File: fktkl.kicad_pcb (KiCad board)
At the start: 2 copper layers, 345.7 x 94.2 mm, 158 parts, among them K1 Esc, K10 Super, K11 2, K12 W, K13 S, K14 X, K15 Alt, K16 3, K17 E, K18 D, K19 C, K2 Tab, K20 4, K21 R, K22 F, K23 V, K24 5, K25 T, K26 G, K27 B, K28 6, K29 Y, K3 Caps, K3.1 SCaps, K30 H, K31 N, K32 Space, K33 7, K34 U, K35 J, K36 M, K37 8, K38 I, K39 K, K4 Shift, K40 ,, K41 9, K42 O, K43 L, K44 ., K45 0, K46 P, K47 ;, K48 /, K49 Ctrl, K5 Ctrl, K50 -, K51 [, K52 ', K53 =, K54 ], K55 Shift, K56 Win, K57 Yen, K58 BS1, K59 BS2, K6 1, K60 \, K61 Enter, K62 Fn, K63 AltGr, K64 Ins, K65 Del, K66 C0, K67 C3, K68 Left, K69 Home, K7 Q, K70 End, K71 C1, K72 Up, K73 Down, K74 PgUp, K75 PgDwn, K76 C2, K77 C4, K78 Right, K8 A, K9 Z

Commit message: changed controller to pro micro
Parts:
- removed the K26 at (156.0, 83.4)
- removed K3.1: SCaps, canadian_footprints:Mx_Alps_125
- removed the K49 at (179.8, 121.5)
- removed the K49 at (260.7, 121.5)
- added G***: LOGO, jan_footprints:dachshund_14.1X8.7_COPPER, F.Cu at (240.0, 119.4)
- added G***: LOGO, jan_footprints:dachshund_181.4x111.4, B.Cu at (186.2, 80.0)
- added K26: Space, canadian_footprints:Mx_Alps_150, F.Cu at (173.8, 116.8)
- added K26: AltGr, canadian_footprints:Mx_Alps_150, F.Cu at (254.8, 116.7)
- added K49: L, canadian_footprints:Mx_Alps_100, F.Cu at (226.2, 78.6)
- added REF**: MountingHole_2.5mm, Mounting_Holes:MountingHole_2.5mm, F.Cu at (100.3, 186.4)
- added Reset1: SW_Push, canadian_footprints:SW_TACT_ALPS_SKQGABE010, B.Cu at (356.4, 50.0)
- K1: value Esc -> SCaps; footprint canadian_footprints:Mx_Alps_100 -> canadian_footprints:Mx_Alps_125
- K10: value Super -> Z
- K11: value 2 -> Super
- K12: value W -> 2
- K13: value S -> W
- K14: value X -> S
- K15: value Alt -> X; footprint canadian_footprints:Mx_Alps_150 -> canadian_footprints:Mx_Alps_100
- K16: value 3 -> Alt; footprint canadian_footprints:Mx_Alps_100 -> canadian_footprints:Mx_Alps_150
- K17: value E -> 3
- K18: value D -> E
- K19: value C -> D
- K2: value Tab -> Esc; footprint canadian_footprints:Mx_Alps_150 -> canadian_footprints:Mx_Alps_100
- K20: value 4 -> C
- K21: value R -> Space; footprint canadian_footprints:Mx_Alps_100 -> MX_Alps_Hybrid:MX-7U-ReversedStabilizers-NoLED
- K22: value F -> 4
- K23: value V -> R
- K24: value 5 -> F
- K25: value T -> V
- K27: value B -> 5
- K28: value 6 -> T
- K29: value Y -> G
- K3: value Caps -> Tab; footprint canadian_footprints:Mx_Alps_175 -> canadian_footprints:Mx_Alps_150
- K30: value H -> B
- K31: value N -> Ctrl; footprint canadian_footprints:Mx_Alps_100 -> canadian_footprints:Mx_Alps_150
- K32: value Space -> 6; footprint MX_Alps_Hybrid:MX-7U-ReversedStabilizers-NoLED -> canadian_footprints:Mx_Alps_100
- K33: value 7 -> Y
- K34: value U -> H
- K35: value J -> N
- K36: value M -> Super
- K37: value 8 -> 7
- K38: value I -> U
- K39: value K -> J
- K4: value Shift -> Caps; footprint canadian_footprints:Mx_Alps_225 -> canadian_footprints:Mx_Alps_175
- K40: value , -> M
- K41: value 9 -> Left
- K42: value O -> 8
- K43: value L -> I
- K44: value . -> K
- K45: value 0 -> ,
- K46: value P -> Down
- K47: value ; -> 9
- K48: value / -> O
- K5: value Ctrl -> Shift; footprint canadian_footprints:Mx_Alps_150 -> canadian_footprints:Mx_Alps_225
- K50: value - -> .
- K51: value [ -> Right
- K52: value ' -> 0
- K53: value = -> P
- K54: value ] -> :
- K55: value Shift -> -; footprint canadian_footprints:Mx_Alps_175 -> canadian_footprints:Mx_Alps_100
- K56: value Win -> [
- K57: value Yen -> "
- K58: value BS1 -> =
- K59: value BS2 -> ]; footprint canadian_footprints:Mx_Alps_200 -> canadian_footprints:Mx_Alps_100
- K6: value 1 -> Ctrl; footprint canadian_footprints:Mx_Alps_100 -> canadian_footprints:Mx_Alps_150
- K60: value \ -> /; footprint canadian_footprints:Mx_Alps_150 -> canadian_footprints:Mx_Alps_100
- K61: value Enter -> Yen; footprint canadian_footprints:Mx_Alps_225 -> canadian_footprints:Mx_Alps_100
- K62: value Fn -> |; footprint canadian_footprints:Mx_Alps_100 -> canadian_footprints:Mx_Alps_150
- K63: value AltGr -> Shift; footprint canadian_footprints:Mx_Alps_150 -> canadian_footprints:Mx_Alps_175
- K64: value Ins -> BS
- K66: value C0 -> Fn
- K67: value C3 -> Ins
- K68: value Left -> Enter; footprint canadian_footprints:Mx_Alps_100 -> canadian_footprints:Mx_Alps_225
- K69: value Home -> C3
- K7: value Q -> 1
- K70: value End -> Home
- K71: value C1 -> C0
- K73: value Down -> PgUp
- K74: value PgUp -> C1
- K75: value PgDwn -> C4
- K76: value C2 -> End
- K77: value C4 -> C2
- K78: value Right -> PgDwn
- K8: value A -> Q
- K9: value Z -> A
- U1: value (none) -> ProMicro; footprint jan_footprints:Teensy_20_wo_front_text -> canadian_footprints:Pro_Micro
- moved U1 275.1 mm to (331.0, 44.7), turned to 180 degrees
- moved K41 133.8 mm to (331.0, 116.7)
- moved D45 132.5 mm to (358.1, 116.6)
- moved D30 131.7 mm to (311.9, 116.7)
- moved D50 119.3 mm to (361.2, 116.6)
- moved K31 118.7 mm to (302.4, 116.7)
- moved D25 116.1 mm to (264.3, 116.7)
- moved K46 116.1 mm to (350.0, 116.7)
- moved K51 116.1 mm to (369.1, 116.7)
- moved D40 109.3 mm to (340.5, 116.7)
- moved D35 90.9 mm to (288.1, 116.7)
- moved D20 87.9 mm to (183.4, 116.7)
- moved K32 84.8 mm to (154.8, 40.5)
- moved K73 82.0 mm to (369.1, 40.5)
- moved D72 81.1 mm to (361.2, 40.4)
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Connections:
- D20 pad 1: /row0 -> /row4
- D21 pad 1: /row1 -> /row0
- D22 pad 1: /row2 -> /row1
- D23 pad 1: /row3 -> /row2
- D24 pad 1: /row0 -> /row3
- D25 pad 1: /row1 -> /row4
- D26 pad 1: /row2 -> /row0
- D27 pad 1: /row3 -> /row1
- D28 pad 1: /row0 -> /row2
- D29 pad 1: /row1 -> /row3
- D30 pad 1: /row2 -> /row4
- D31 pad 1: /row3 -> /row0
- D32 pad 1: /row4 -> /row1
- D33 pad 1: /row0 -> /row2
- D34 pad 1: /row1 -> /row3
- D35 pad 1: /row2 -> /row4
- D36 pad 1: /row3 -> /row0
- D37 pad 1: /row0 -> /row1
- D38 pad 1: /row1 -> /row2
- D39 pad 1: /row2 -> /row3
- D40 pad 1: /row3 -> /row4
- D45 pad 1: /row0 -> /row4
- D46 pad 1: /row1 -> /row0
- D47 pad 1: /row2 -> /row1
- D48 pad 1: /row3 -> /row2
- D49 pad 1: /row4 -> /row3
- D50 pad 1: /row0 -> /row4
- D51 pad 1: /row1 -> /row5
- D52 pad 1: /row2 -> /row6
- D53 pad 1: /row0 -> /row7
- D54 pad 1: /row1 -> /row5
- D55 pad 1: /row3 -> /row6
- D56 pad 1: /row4 -> /row7
- D57 pad 1: /row2 -> /row5
- D58 pad 1: /row0 -> /row6
- D59 pad 1: /row1 -> /row7
- D60 pad 1: /row2 -> /row5
- D61 pad 1: /row3 -> /row6
- D62 pad 1: /row4 -> /row7
- D63 pad 1: /row0 -> /row5
- D64 pad 1: /row1 -> /row6
- D65 pad 1: /row2 -> /row7
- D66 pad 1: /row3 -> /row5
- D67 pad 1: /row4 -> /row6
- D68 pad 1: /row0 -> /row7
- D69 pad 1: /row1 -> /row5
- D70 pad 1: /row2 -> /row6
- D71 pad 1: /row3 -> /row7
- D72 pad 1: /row4 -> /row5
- D73 pad 1: /row0 -> /row6
- D74 pad 1: /row1 -> /row7
- D75 pad 1: /row2 -> /row5
- D76 pad 1: /row3 -> /row6
- D77 pad 1: /row4 -> /row5
- K1 pad 2: Net-(D1-Pad2) -> Net-(D3-Pad2)
- K10 pad 2: Net-(D10-Pad2) -> Net-(D9-Pad2)
- K11 pad 1: /col2 -> /col1
- K11 pad 2: Net-(D11-Pad2) -> Net-(D10-Pad2)
- K12 pad 2: Net-(D12-Pad2) -> Net-(D11-Pad2)
- K13 pad 2: Net-(D13-Pad2) -> Net-(D12-Pad2)
- K14 pad 2: Net-(D14-Pad2) -> Net-(D13-Pad2)
- K15 pad 2: Net-(D15-Pad2) -> Net-(D14-Pad2)
- K16 pad 1: /col3 -> /col2
- K16 pad 2: Net-(D16-Pad2) -> Net-(D15-Pad2)
- K17 pad 2: Net-(D17-Pad2) -> Net-(D16-Pad2)
- K18 pad 2: Net-(D18-Pad2) -> Net-(D17-Pad2)
- K19 pad 2: Net-(D19-Pad2) -> Net-(D18-Pad2)
- K2 pad 2: Net-(D2-Pad2) -> Net-(D1-Pad2)
- K20 pad 1: /col4 -> /col3
- K20 pad 2: Net-(D20-Pad2) -> Net-(D19-Pad2)
- K21 pad 1: /col4 -> /col3
- K21 pad 2: Net-(D21-Pad2) -> Net-(D20-Pad2)
- K22 pad 2: Net-(D22-Pad2) -> Net-(D21-Pad2)
- K23 pad 2: Net-(D23-Pad2) -> Net-(D22-Pad2)
- K24 pad 1: /col5 -> /col4
- K24 pad 2: Net-(D24-Pad2) -> Net-(D23-Pad2)
- K25 pad 1: /col5 -> /col4
- K25 pad 2: Net-(D25-Pad2) -> Net-(D24-Pad2)
- K27 pad 2: Net-(D27-Pad2) -> Net-(D26-Pad2)
- K28 pad 1: /col6 -> /col5
- K28 pad 2: Net-(D28-Pad2) -> Net-(D27-Pad2)
- K29 pad 1: /col6 -> /col5
- K29 pad 2: Net-(D29-Pad2) -> Net-(D28-Pad2)
- K3 pad 2: Net-(D3-Pad2) -> Net-(D2-Pad2)
- K30 pad 1: /col6 -> /col5
- K30 pad 2: Net-(D30-Pad2) -> Net-(D29-Pad2)
- K31 pad 1: /col6 -> /col5
- K31 pad 2: Net-(D31-Pad2) -> Net-(D30-Pad2)
- K32 pad 2: Net-(D32-Pad2) -> Net-(D31-Pad2)
- K33 pad 1: /col7 -> /col6
- K33 pad 2: Net-(D33-Pad2) -> Net-(D32-Pad2)
- K34 pad 1: /col7 -> /col6
- K34 pad 2: Net-(D34-Pad2) -> Net-(D33-Pad2)
- K35 pad 1: /col7 -> /col6
- K35 pad 2: Net-(D35-Pad2) -> Net-(D34-Pad2)
- K36 pad 1: /col7 -> /col6
- K36 pad 2: Net-(D36-Pad2) -> Net-(D35-Pad2)
- K37 pad 1: /col8 -> /col7
- K37 pad 2: Net-(D37-Pad2) -> Net-(D36-Pad2)
- K38 pad 1: /col8 -> /col7
- K38 pad 2: Net-(D38-Pad2) -> Net-(D37-Pad2)
- K39 pad 1: /col8 -> /col7
- K39 pad 2: Net-(D39-Pad2) -> Net-(D38-Pad2)
- K4 pad 2: Net-(D4-Pad2) -> Net-(D3-Pad2)
- K40 pad 1: /col8 -> /col7
- K40 pad 2: Net-(D40-Pad2) -> Net-(D39-Pad2)
- K41 pad 1: /col9 -> /col7
- K41 pad 2: Net-(D41-Pad2) -> Net-(D40-Pad2)
- K42 pad 1: /col9 -> /col8
- K42 pad 2: Net-(D42-Pad2) -> Net-(D41-Pad2)
- K43 pad 1: /col9 -> /col8
- K43 pad 2: Net-(D43-Pad2) -> Net-(D42-Pad2)
- K44 pad 1: /col9 -> /col8
- K44 pad 2: Net-(D44-Pad2) -> Net-(D43-Pad2)
- K45 pad 1: /col10 -> /col8
- K45 pad 2: Net-(D45-Pad2) -> Net-(D44-Pad2)
- K46 pad 1: /col10 -> /col8
- K46 pad 2: Net-(D46-Pad2) -> Net-(D45-Pad2)
- K47 pad 1: /col10 -> /col9
- K47 pad 2: Net-(D47-Pad2) -> Net-(D46-Pad2)
- K48 pad 1: /col10 -> /col9
- K48 pad 2: Net-(D48-Pad2) -> Net-(D47-Pad2)
- K5 pad 2: Net-(D5-Pad2) -> Net-(D4-Pad2)
- K50 pad 1: /col11 -> /col9
- K50 pad 2: Net-(D50-Pad2) -> Net-(D49-Pad2)
- K51 pad 1: /col11 -> /col9
- K51 pad 2: Net-(D51-Pad2) -> Net-(D50-Pad2)
- K52 pad 1: /col11 -> /col0
- K52 pad 2: Net-(D52-Pad2) -> Net-(D51-Pad2)
- K53 pad 1: /col12 -> /col0
- K53 pad 2: Net-(D53-Pad2) -> Net-(D52-Pad2)
- K54 pad 1: /col12 -> /col0
- K54 pad 2: Net-(D54-Pad2) -> Net-(D53-Pad2)
- K55 pad 1: /col12 -> /col1
- K55 pad 2: Net-(D55-Pad2) -> Net-(D54-Pad2)
- K56 pad 1: /col12 -> /col1
- K56 pad 2: Net-(D56-Pad2) -> Net-(D55-Pad2)
- K57 pad 1: /col12 -> /col1
- K57 pad 2: Net-(D57-Pad2) -> Net-(D56-Pad2)
- K58 pad 1: /col13 -> /col2
- K58 pad 2: Net-(D58-Pad2) -> Net-(D57-Pad2)
- K59 pad 1: /col13 -> /col2
- K6 pad 1: /col1 -> /col0
- K6 pad 2: Net-(D6-Pad2) -> Net-(D5-Pad2)
- K60 pad 1: /col13 -> /col2
- K61 pad 1: /col13 -> /col3
- K62 pad 1: /col13 -> /col3
- K63 pad 1: /col13 -> /col3
- K64 pad 1: /col14 -> /col4
- K65 pad 1: /col14 -> /col5
- K66 pad 1: /col14 -> /col4
- K67 pad 1: /col14 -> /col5
- K68 pad 1: /col14 -> /col4
- K69 pad 1: /col15 -> /col6
- K7 pad 2: Net-(D7-Pad2) -> Net-(D6-Pad2)
- K70 pad 1: /col15 -> /col6
- K71 pad 1: /col15 -> /col6
- K72 pad 1: /col15 -> /col7
- K73 pad 1: /col15 -> /col7
- K74 pad 1: /col16 -> /col7
- K75 pad 1: /col16 -> /col9
- K76 pad 1: /col16 -> /col8
- K77 pad 1: /col16 -> /col9
- K78 pad 1: /col16 -> /col9
- K8 pad 2: Net-(D8-Pad2) -> Net-(D7-Pad2)
- K9 pad 2: Net-(D9-Pad2) -> Net-(D8-Pad2)
- U1 pad 1: GND -> Net-(U1-Pad1)
- U1 pad 10: /col9 -> /col5
- U1 pad 11: /col8 -> /col6
- U1 pad 12: /col7 -> /row6
- U1 pad 13: /col2 -> /row0
- U1 pad 15: Net-(U1-Pad15) -> GND
- U1 pad 16: Net-(U1-Pad16) -> GND
- U1 pad 17: /col1 -> /row2
- U1 pad 18: Net-(U1-Pad18) -> /row3
- U1 pad 19: /col16 -> /row4
- U1 pad 2: /col0 -> GND
- U1 pad 20: /col6 -> /col0
- U1 pad 21: /col5 -> /col1
- U1 pad 22: /col4 -> /col2
- U1 pad 24: Net-(U1-Pad24) -> /row1
- U1 pad 3: /row0 -> Net-(Reset1-Pad2)
- U1 pad 4: /col15 -> VCC
- U1 pad 5: /col14 -> /col7
- U1 pad 6: /col13 -> /row5
- U1 pad 7: /col12 -> /col4
- U1 pad 8: /col11 -> /col9
- U1 pad 9: /col10 -> /col8
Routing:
- net /col16: track 393.4 -> 0.00 mm
- net /col15: track 388.8 -> 0.00 mm
- net /col14: track 366.9 -> 0.00 mm
- net /col13: track 358.2 -> 0.00 mm
- net /col12: track 337.6 -> 0.00 mm
- net /col4: track 148.2 -> 472.9 mm, vias 0 -> 3
- net /col0: track 92.4 -> 412.7 mm, vias 0 -> 2
- net /col2: track 115.4 -> 411.6 mm, vias 0 -> 2
- net /col1: track 102.1 -> 396.9 mm, vias 0 -> 2
- net /col3: track 131.7 -> 408.2 mm, vias 0 -> 2
- net /col10: track 274.4 -> 0.00 mm
- net /col11: track 254.5 -> 0.00 mm
- net /col5: track 164.7 -> 379.1 mm, vias 0 -> 2
- net /col7: track 188.7 -> 383.6 mm, vias 0 -> 3
- net /col6: track 203.1 -> 384.9 mm, vias 0 -> 3
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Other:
- board size 345.7 x 94.2 mm -> 342.6 x 94.5 mm
- board text added: "fkltkl v0.1"
- board text added: "https://github.com/pika-pi/fkltkl"

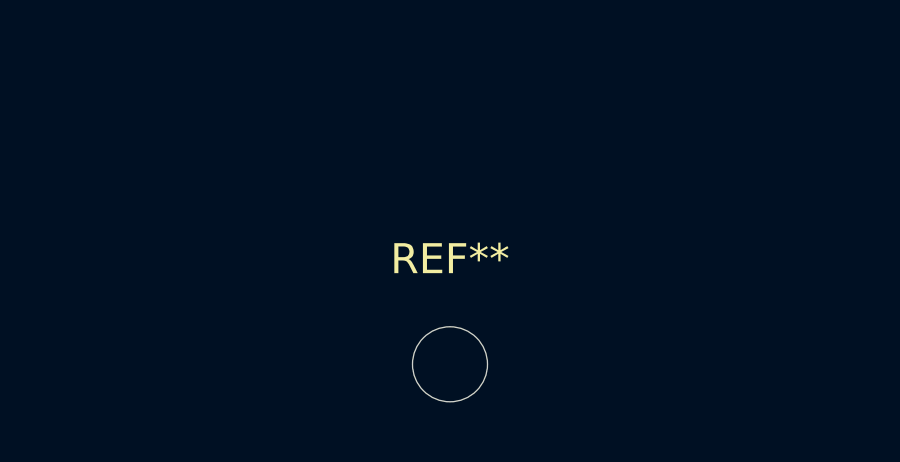
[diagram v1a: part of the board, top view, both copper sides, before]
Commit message: removed unused mounting hole
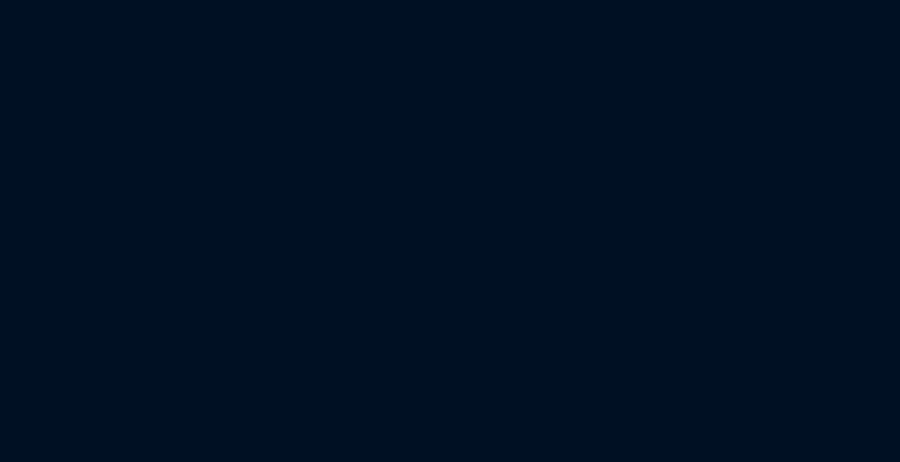
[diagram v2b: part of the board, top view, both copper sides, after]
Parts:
- removed REF**: MountingHole_2.5mm, Mounting_Holes:MountingHole_2.5mm
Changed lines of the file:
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@@
     (links 548)
     (no_connects 0)
-    (area 33.452999 30.912999 376.249001 125.551001)
+    (area 30.805779 28.7814 378.767951 191.011)
     (thickness 1.6)
     (drawings 10)
     (tracks 718)
     (zones 0)
-    (modules 161)
+    (modules 160)
     (nets 101)
   )
@@
       (xy -64.49198 39.840938)) (layer B.SilkS) (width 0.01))
   )
-  (module Mounting_Holes:MountingHole_2.5mm (layer F.Cu)
-    (at 100.33 186.436)
-    (descr "Mounting Hole 2.5mm, no annular")
-    (tags "mounting hole 2.5mm no annular")
-    (attr virtual)
-    (fp_text reference REF** (at 0 -3.5) (layer F.SilkS)
-      (effects (font (size 1 1) (thickness 0.15)))
-    )
-    (fp_text value MountingHole_2.5mm (at 0 3.5) (layer F.Fab)
-      (effects (font (size 1 1) (thickness 0.15)))
-    )
-    (fp_text user %R (at 0.3 0) (layer F.Fab)
-      (effects (font (size 1 1) (thickness 0.15)))
-    )
-    (fp_circle (center 0 0) (end 2.5 0) (layer Cmts.User) (width 0.15))
-    (fp_circle (center 0 0) (end 2.75 0) (layer F.CrtYd) (width 0.05))
-    (pad 1 np_thru_hole circle (at 0 0) (size 2.5 2.5) (drill 2.5) (layers *.Cu *.Mask))
-  )
   (gr_line (start 375.158 125.476) (end 34.544 125.476) (angle 90) (layer Edge.Cuts) (width 0.15))
